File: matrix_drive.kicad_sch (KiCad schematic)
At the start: 0 parts

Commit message: [#72133] Add LED matrix
Signed-off-by: Dawid Lentka <dlentka@antmicro.com>
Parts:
- added U? (x4): LED_Matrix_KWM-50571AGB, symbol antmicroModules:LED_Matrix_KWM-50571AGB
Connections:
- new net ColumnDrive1: U?.13 (C1), U?.13 (C1)
- new net ColumnDrive10: U?.6 (C5), U?.6 (C5)
- new net ColumnDrive2: U?.3 (C2), U?.3 (C2)
- new net ColumnDrive3: U?.11 (C3), U?.11 (C3), U?.4 (C3), U?.4 (C3)
- new net ColumnDrive4: U?.10 (C4), U?.10 (C4)
- new net ColumnDrive5: U?.6 (C5), U?.6 (C5)
- new net ColumnDrive6: U?.13 (C1), U?.13 (C1)
- new net ColumnDrive7: U?.3 (C2), U?.3 (C2)
- new net ColumnDrive8: U?.11 (C3), U?.11 (C3), U?.4 (C3), U?.4 (C3)
- new net ColumnDrive9: U?.10 (C4), U?.10 (C4)
- new net RowDrive1: U?.9 (A1), U?.9 (A1)
- new net RowDrive10: U?.8 (A3), U?.8 (A3)
- new net RowDrive11: U?.12 (A4), U?.12 (A4), U?.5 (A4), U?.5 (A4)
- new net RowDrive12: U?.1 (A5), U?.1 (A5)
- new net RowDrive13: U?.7 (A6), U?.7 (A6)
- new net RowDrive14: U?.2 (A7), U?.2 (A7)
- new net RowDrive2: U?.14 (A2), U?.14 (A2)
- new net RowDrive3: U?.8 (A3), U?.8 (A3)
- new net RowDrive4: U?.12 (A4), U?.12 (A4), U?.5 (A4), U?.5 (A4)
- new net RowDrive5: U?.1 (A5), U?.1 (A5)
- new net RowDrive6: U?.7 (A6), U?.7 (A6)
- new net RowDrive7: U?.2 (A7), U?.2 (A7)
- new net RowDrive8: U?.9 (A1), U?.9 (A1)
- new net RowDrive9: U?.14 (A2), U?.14 (A2)

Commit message: [#72133] Unify sheet size
Signed-off-by: Dawid Lentka <dlentka@antmicro.com>
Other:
- title: (none) -> LED Panel Board
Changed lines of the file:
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@@
 	(generator_version "8.0")
 	(paper "A4")
+	(title_block
+		(title "LED Panel Board")
+		(date "28.01.2025")
+		(rev "1.0.0")
+	)
 	(junction
 		(at 80.01 123.19)

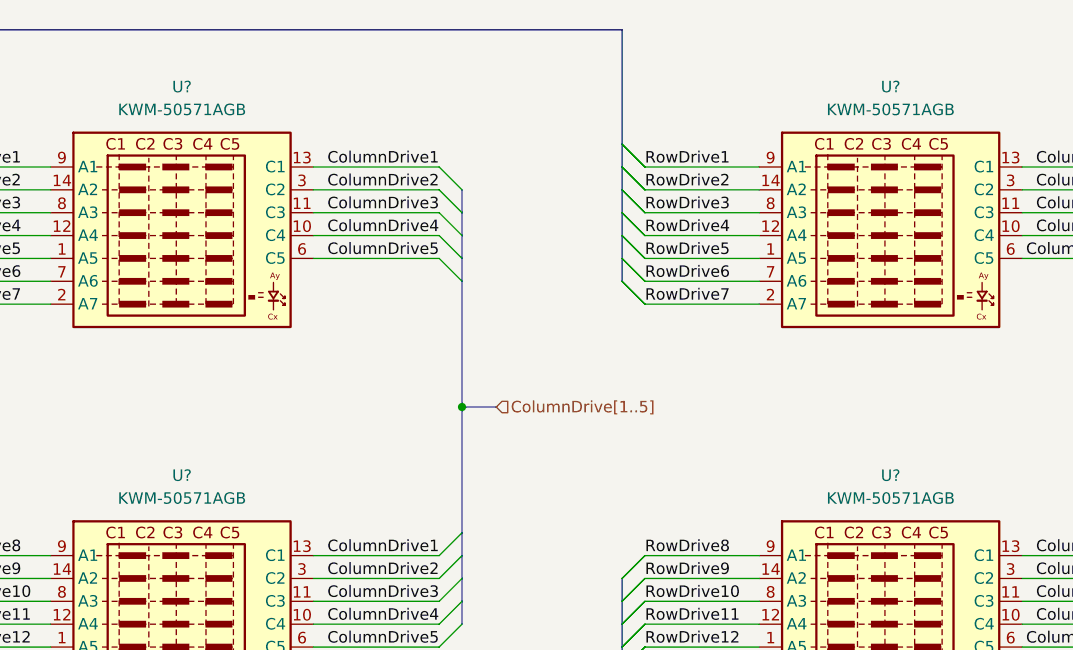
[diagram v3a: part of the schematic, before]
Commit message: [#72133] Annotate schematics
Signed-off-by: Dawid Lentka <dlentka@antmicro.com>
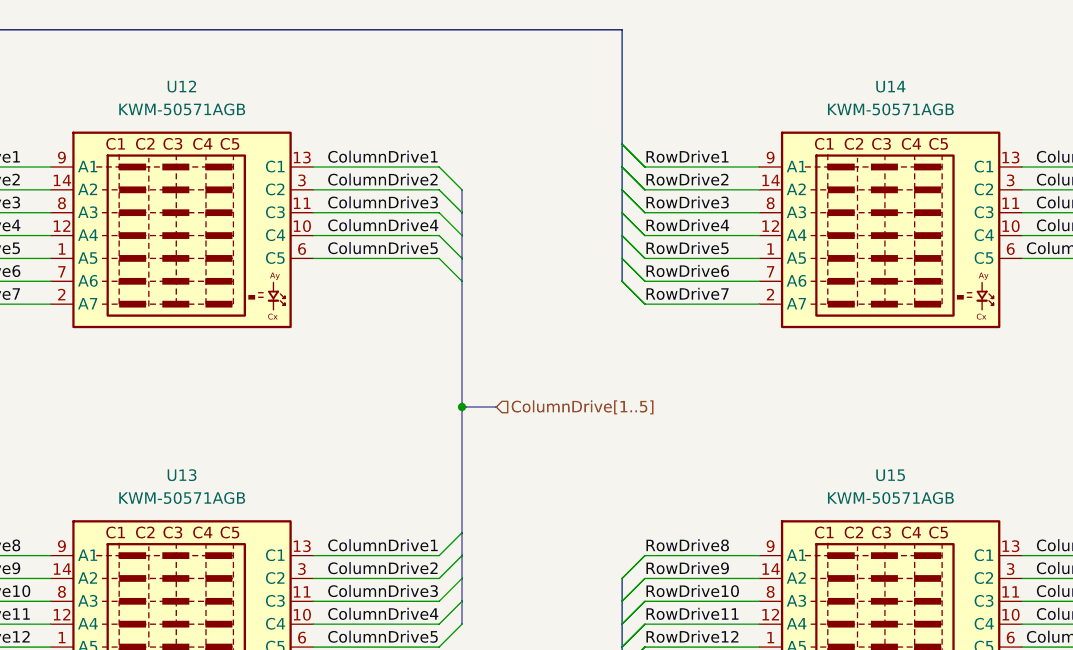
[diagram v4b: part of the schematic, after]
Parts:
- gave numbers to parts that had none: 4
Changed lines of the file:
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@@
 		(dnp no)
 		(fields_autoplaced yes)
-		(property "Reference" "U?"
+		(property "Reference" "U15"
 			(at 188.595 92.71 0)
 			(effects
@@
 			(project "led-panel"
 				(path "/a86e1cab-ea0a-45e6-9194-d44b0d5c9450/4a8c8e0e-1171-44e1-a868-b4d68419a221"
-					(reference "U?")
+					(reference "U15")
 					(unit 1)
 				)
@@
 		(dnp no)
 		(fields_autoplaced yes)
-		(property "Reference" "U?"
+		(property "Reference" "U14"
 			(at 188.595 49.53 0)
 			(effects
@@
 			(project "led-panel"
 				(path "/a86e1cab-ea0a-45e6-9194-d44b0d5c9450/4a8c8e0e-1171-44e1-a868-b4d68419a221"
-					(reference "U?")
+					(reference "U14")
 					(unit 1)
 				)
@@
 		(dnp no)
 		(fields_autoplaced yes)
-		(property "Reference" "U?"
+		(property "Reference" "U12"
 			(at 109.855 49.53 0)
 			(effects
@@
 			(project "led-panel"
 				(path "/a86e1cab-ea0a-45e6-9194-d44b0d5c9450/4a8c8e0e-1171-44e1-a868-b4d68419a221"
-					(reference "U?")
+					(reference "U12")
 					(unit 1)
 				)
@@
 		(dnp no)
 		(fields_autoplaced yes)
-		(property "Reference" "U?"
+		(property "Reference" "U13"
 			(at 109.855 92.71 0)
 			(effects
@@
 			(project "led-panel"
 				(path "/a86e1cab-ea0a-45e6-9194-d44b0d5c9450/4a8c8e0e-1171-44e1-a868-b4d68419a221"
-					(reference "U?")
+					(reference "U13")
 					(unit 1)
 				)

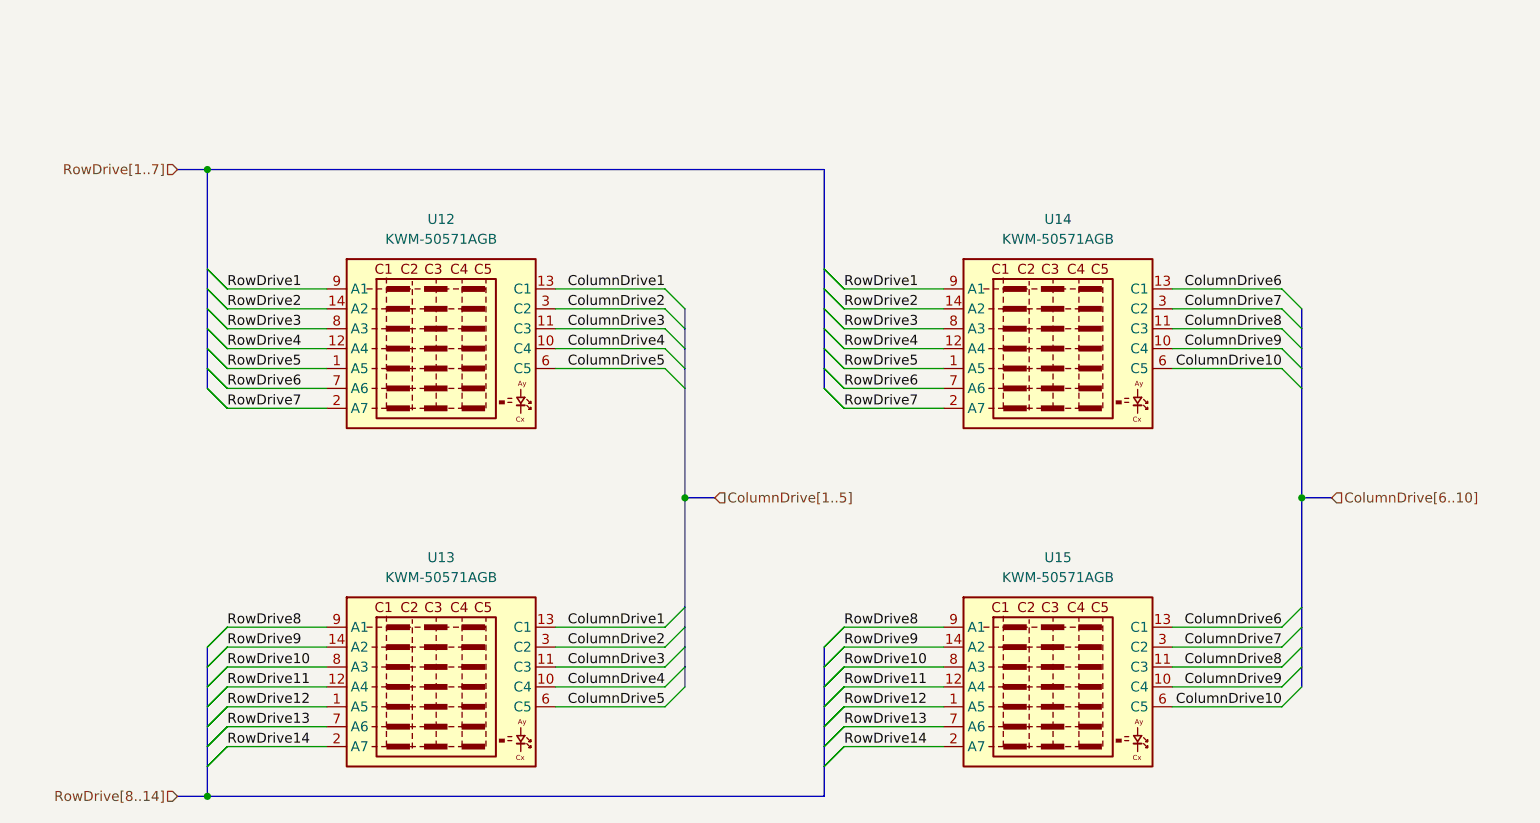
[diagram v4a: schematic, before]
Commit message: [#72133] Update symbol from lib
Signed-off-by: Dawid Lentka <dlentka@antmicro.com>
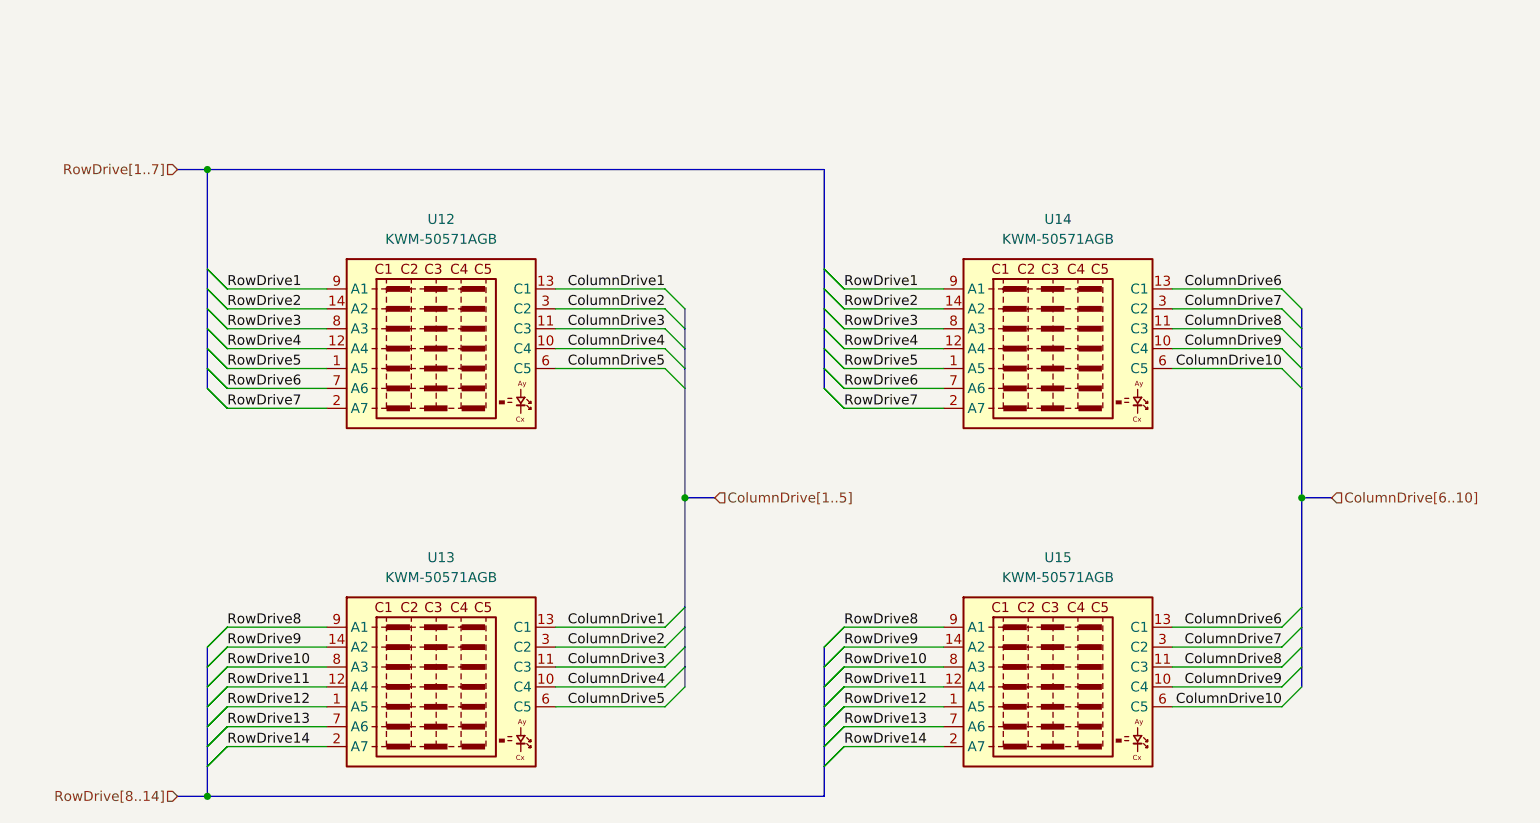
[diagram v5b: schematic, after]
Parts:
- U12, U13, U14, U15: footprint (none) -> antmicro-footprints:LED_Matrix_KWM_50571AGB
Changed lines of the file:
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@@
 			)
 		)
-		(property "Footprint" ""
+		(property "Footprint" "antmicro-footprints:LED_Matrix_KWM_50571AGB"
 			(at 217.17 111.76 0)
 			(effects
@@
 			)
 		)
-		(property "Footprint" ""
+		(property "Footprint" "antmicro-footprints:LED_Matrix_KWM_50571AGB"
 			(at 217.17 68.58 0)
 			(effects
@@
 			)
 		)
-		(property "Footprint" ""
+		(property "Footprint" "antmicro-footprints:LED_Matrix_KWM_50571AGB"
 			(at 138.43 68.58 0)
 			(effects
@@
 			)
 		)
-		(property "Footprint" ""
+		(property "Footprint" "antmicro-footprints:LED_Matrix_KWM_50571AGB"
 			(at 138.43 111.76 0)
 			(effects

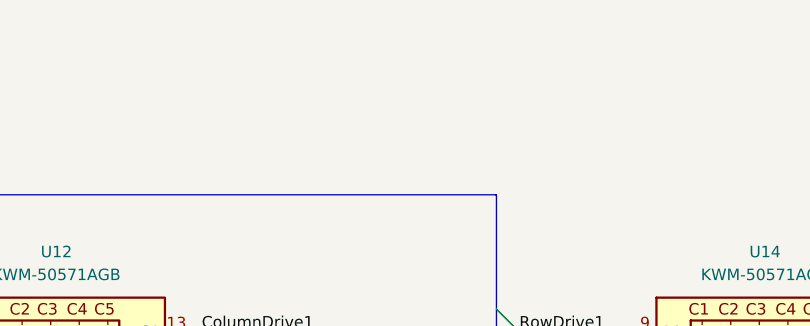
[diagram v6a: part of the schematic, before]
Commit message: [#72133] Add captions to schematic sheets
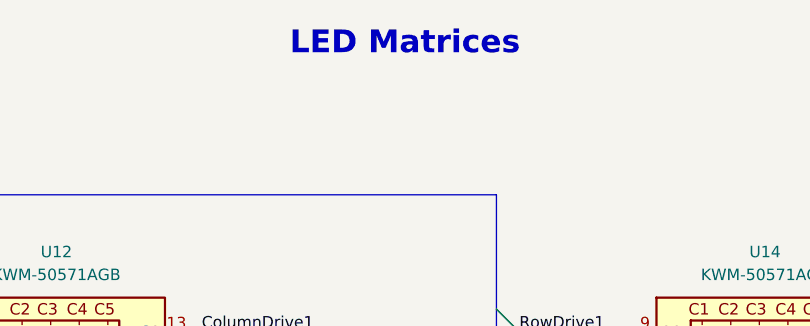
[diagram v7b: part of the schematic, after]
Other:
- note added: "LED Matrices"
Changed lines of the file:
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@@
+		)
+	)
+	(text "LED Matrices"
+		(exclude_from_sim no)
+		(at 148.59 26.416 0)
+		(effects
+			(font
+				(size 2.54 2.54)
+				(thickness 0.508)
+				(bold yes)
+			)
 		)
 	)
